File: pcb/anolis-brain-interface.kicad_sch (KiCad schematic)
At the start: 2 parts, among them U1 RHD2216, U2 Setebos-I

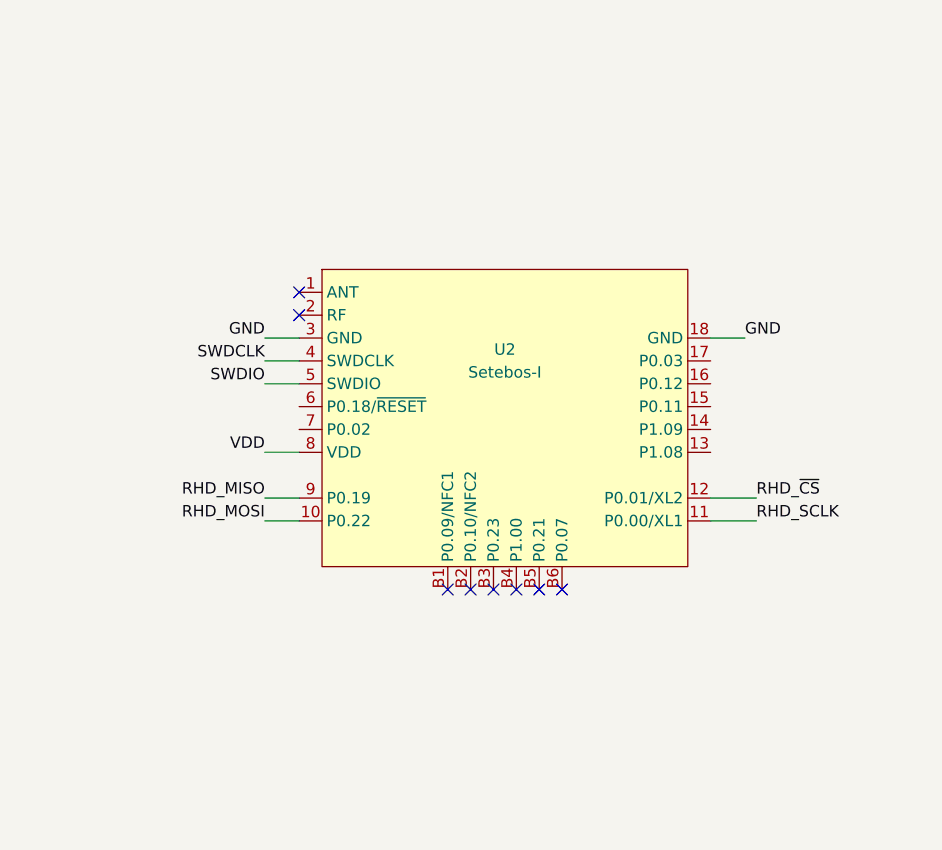
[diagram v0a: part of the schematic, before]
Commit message: Added uSD socket.
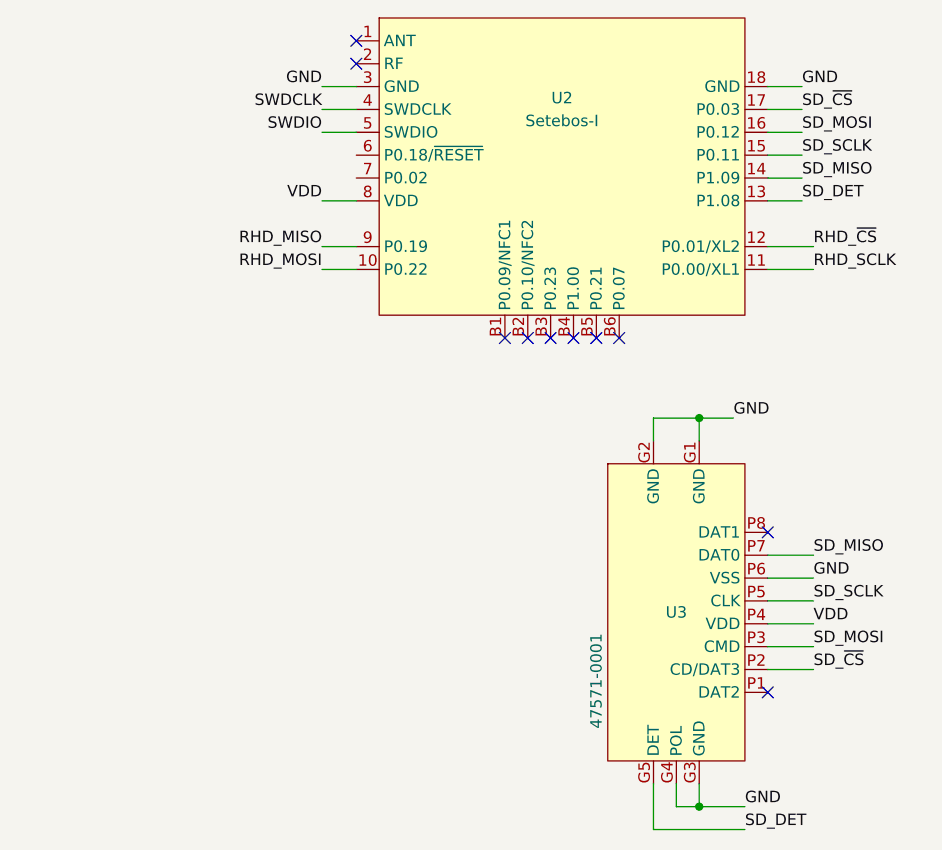
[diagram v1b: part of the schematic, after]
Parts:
- added U3: 47571-0001, sd:475710001, symbol sd:475710001
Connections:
- net GND: now also U3.G1 (GND), U3.G2 (GND), U3.G3 (GND), U3.G4 (POL), U3.P6 (VSS)
- net VDD: now also U3.P4 (VDD)
- net SD_DET: now reaches U2.13 (P1.08)
- net SD_DET: now also U3.G5 (DET)
- net SD_MISO: now reaches U2.14 (P1.09)
- net SD_MISO: now also U3.P7 (DAT0)
- net SD_SCLK: now reaches U2.15 (P0.11)
- net SD_SCLK: now also U3.P5 (CLK)
- net SD_MOSI: now reaches U2.16 (P0.12)
- net SD_MOSI: now also U3.P3 (CMD)
- net SD_~{CS}: now reaches U2.17 (P0.03)
- net SD_~{CS}: now also U3.P2 (CD/DAT3)
- no-connect marks 12 -> 14
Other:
- moved on the sheet: U2

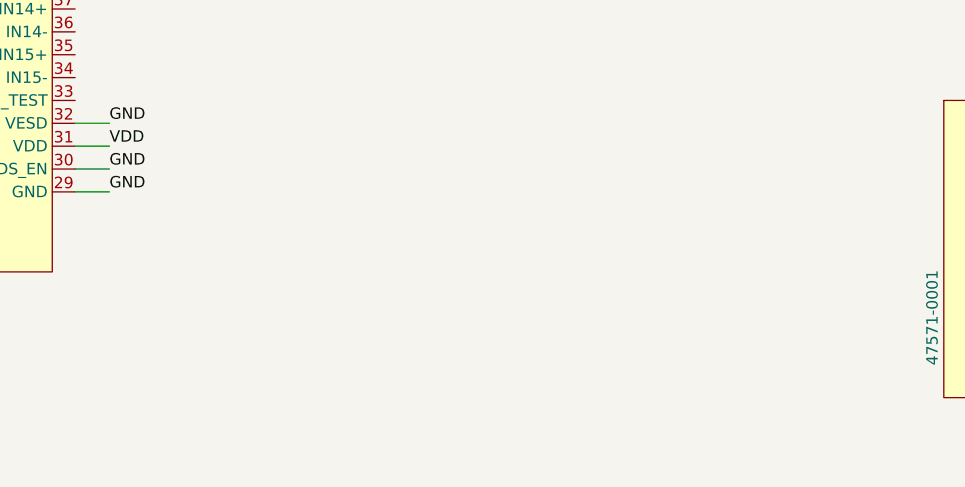
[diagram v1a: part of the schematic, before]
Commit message: Added power supply.
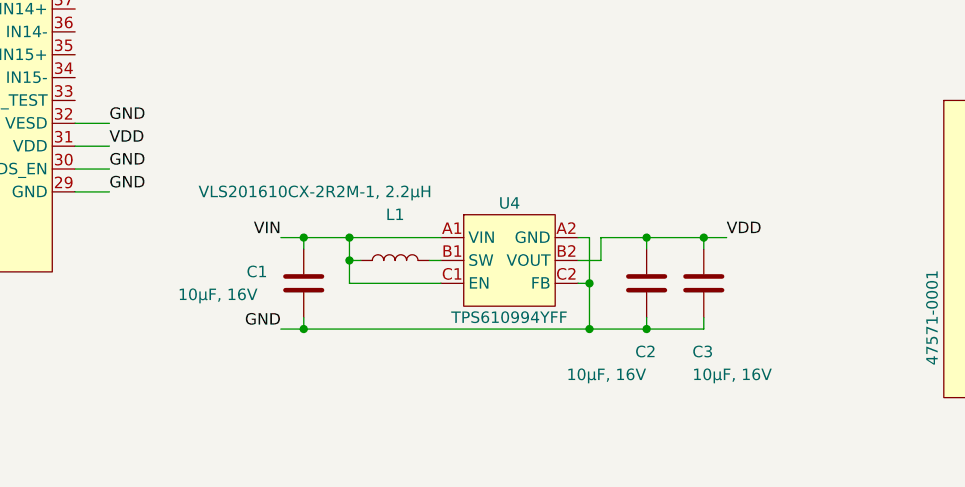
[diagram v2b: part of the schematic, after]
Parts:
- added C1, C2, C3: 10µF, 16V, Capacitor_SMD:C_0603_1608Metric, symbol Device:C
- added L1: VLS201610CX-2R2M-1, 2.2µH, Inductor_SMD:L_Murata_DFE201610P, symbol Device:L
- added U4: TPS610994YFF, Package_BGA:Texas_DSBGA-6_0.855x1.255mm_Layout2x3_P0.4mm_LevelC, symbol tps61099:TPS61099
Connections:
- net GND: now also C1.2, C2.2, C3.2, U4.A2 (GND), U4.C2 (FB)
- net VDD: now also C2.1, C3.1, U4.B2 (VOUT)
- new net: L1.2, U4.B1 (SW)
- new net VIN: C1.1, L1.1, U4.A1 (VIN), U4.C1 (EN)

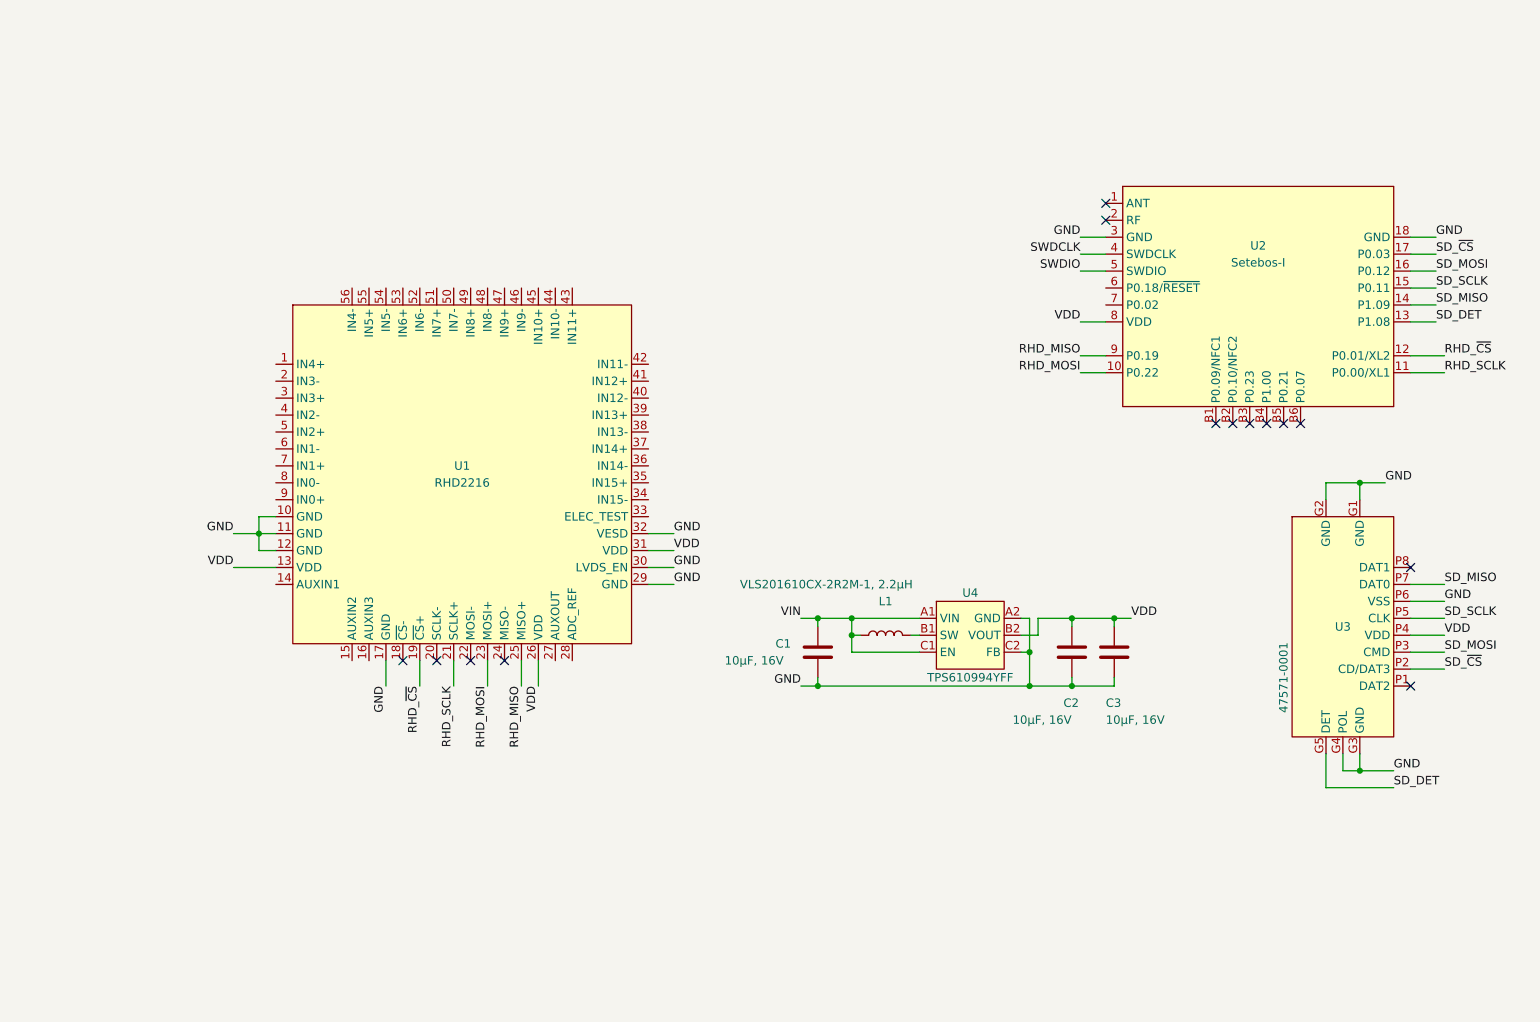
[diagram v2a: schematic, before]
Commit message: Added capacitors.
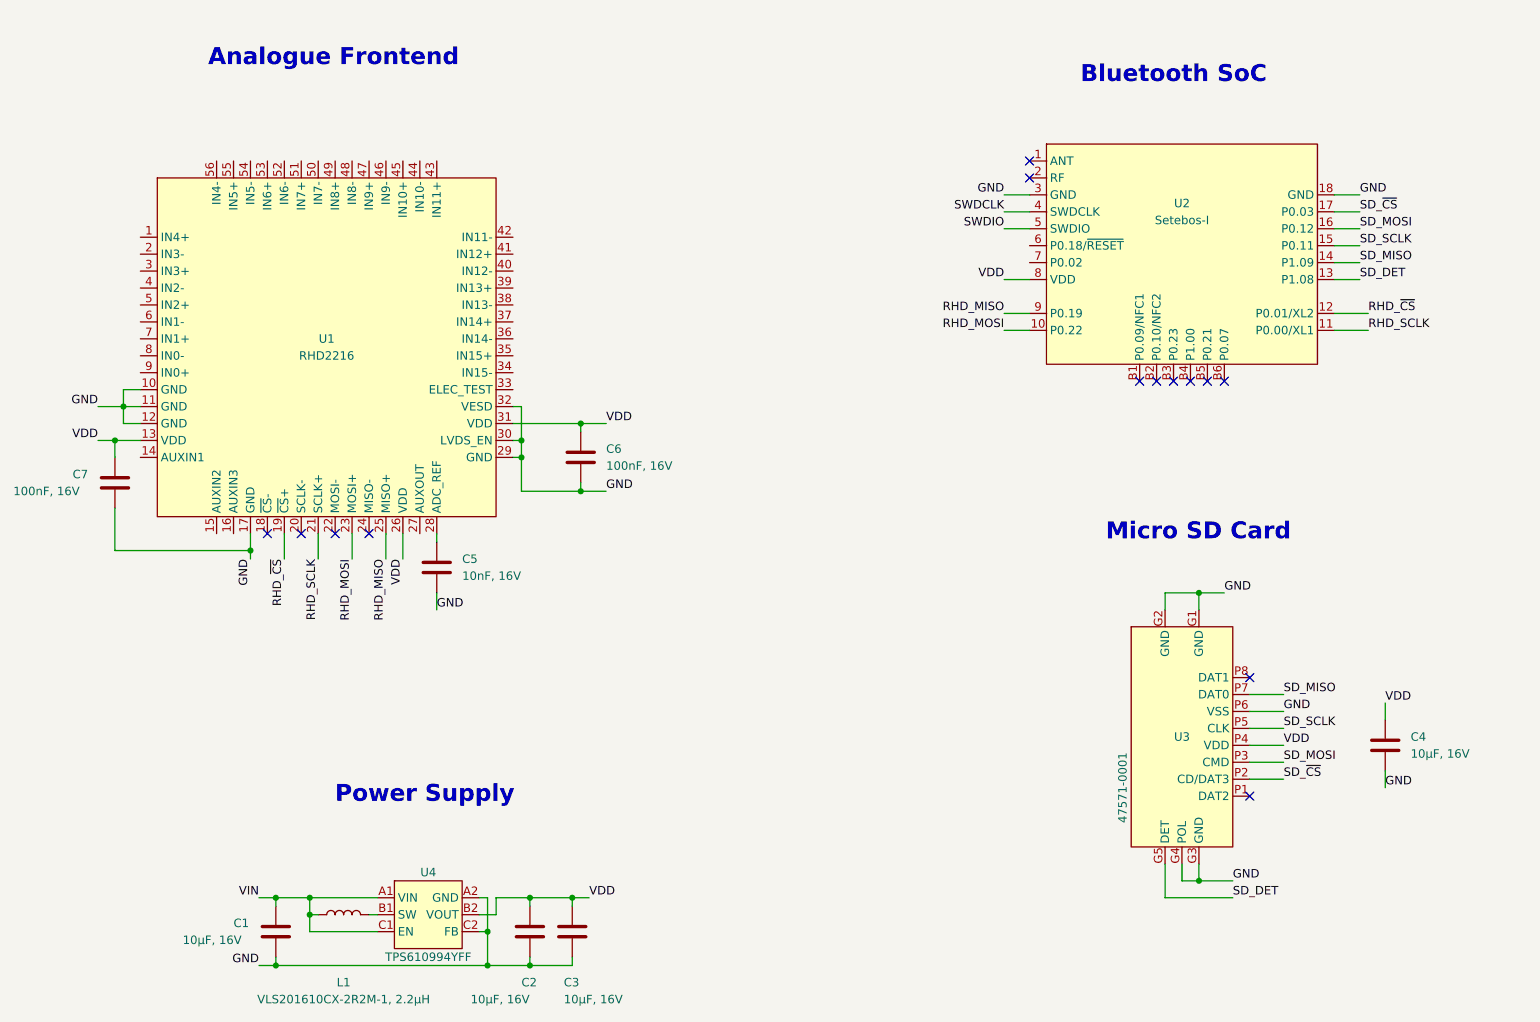
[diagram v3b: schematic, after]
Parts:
- added C4: 10µF, 16V, Capacitor_SMD:C_0603_1608Metric, symbol Device:C
- added C5: 10nF, 16V, Capacitor_SMD:C_0402_1005Metric, symbol Device:C
- added C6, C7: 100nF, 16V, Capacitor_SMD:C_0402_1005Metric, symbol Device:C
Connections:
- net GND: now also C4.2, C5.2, C6.2, C7.2
- net VDD: now also C4.1, C6.1, C7.1
- net at U1.28 (ADC_REF): now also C5.1
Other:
- note added: "Analogue Frontend"
- note added: "Bluetooth SoC"
- note added: "Micro SD Card"
- note added: "Power Supply"
- moved on the sheet: C1, C2, C3, L1, U1, U2, U3, U4

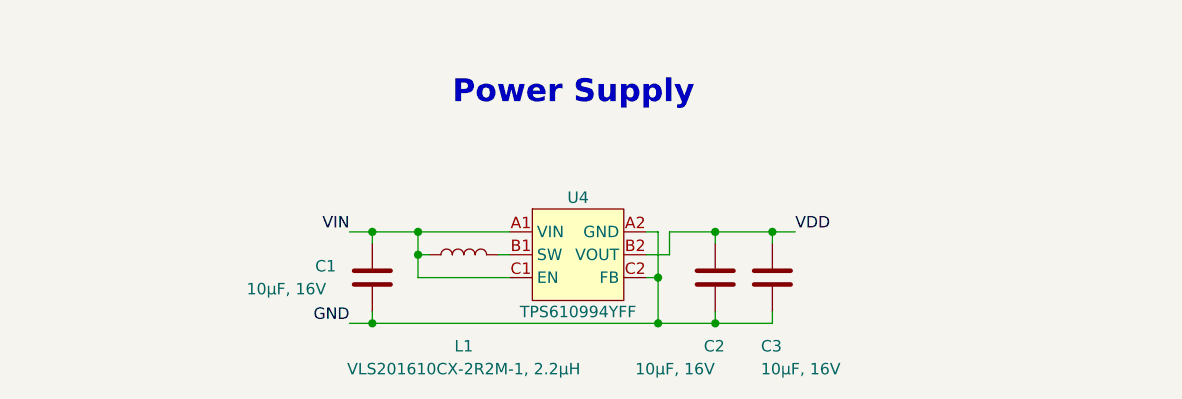
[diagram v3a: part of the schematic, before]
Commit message: Added battery connector.
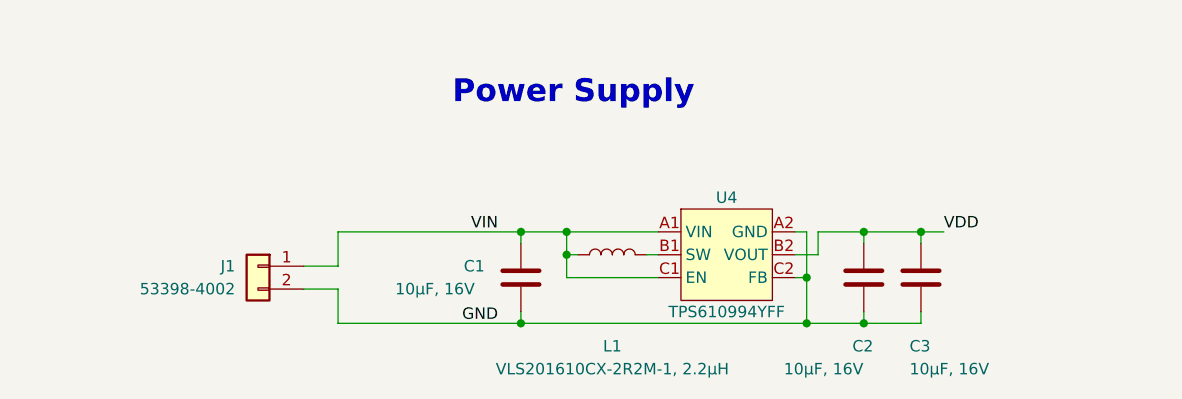
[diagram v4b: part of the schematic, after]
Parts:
- added J1: 53398-4002, Connector_Molex:Molex_PicoBlade_53398-0271_1x02-1MP_P1.25mm_Vertical, symbol Connector_Generic:Conn_01x02
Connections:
- net GND: now also J1.2 (Pin_2)
- net VIN: now also J1.1 (Pin_1)
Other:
- title: (none) -> Anolis Brain Interface
- moved on the sheet: C1, C2, C3, L1, U4

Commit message: Diode added.
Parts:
- added D1: PMEG2010EJ, Diode_SMD:D_SOD-323F, symbol Diode:PMEG2010EJ
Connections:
- net VIN: now also D1.1 (K); no longer J1.1 (Pin_1)
- new net: D1.2 (A), J1.1 (Pin_1)
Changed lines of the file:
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@@
+    (stroke (width 0) (type default))
+  )
+  (wire (pts (xy 59.69 154.94) (xy 68.58 154.94))
     (stroke (width 0) (type default))
   )
@@
     (stroke (width 0) (type default))
   )
-  (wire (pts (xy 48.26 154.94) (xy 68.58 154.94))
+  (wire (pts (xy 48.26 154.94) (xy 52.07 154.94))
     (stroke (width 0) (type default))
   )
@@
         )
       )
+    )
+  )
+  (symbol (lib_id "Diode:PMEG2010EJ") (at 55.88 154.94 180) (unit 1)
+    (in_bom yes) (on_board yes) (dnp no) (fields_autoplaced)
+    (property "Reference" "D1" (at 56.1975 148.59 0)
+      (effects (font (size 1.27 1.27)))
+    )
+    (property "Value" "PMEG2010EJ" (at 56.1975 151.13 0)
+      (effects (font (size 1.27 1.27)))
+    )
+    (property "Footprint" "Diode_SMD:D_SOD-323F" (at 55.88 150.495 0)
+      (effects (font (size 1.27 1.27)) hide)
+    )
+    (property "Datasheet" "https://assets.nexperia.com/documents/data-sheet/PMEG2010EH_EJ_ET.pdf" (at 55.88 154.94 0)
+      (effects (font (size 1.27 1.27)) hide)
+    )
+    (pin "1")
+    (pin "2")
+    (instances
+      (project "anolis-brain-interface"
+        (path "/2073a088-93fe-4857-bf83-cba62e9d9994"
+          (reference "D1") (unit 1)
+        )
+      )

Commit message: Segmented draft.
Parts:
- removed C4: 10µF, 16V, Capacitor_SMD:C_0603_1608Metric, symbol Device:C
- removed U3: 47571-0001, sd:475710001, symbol sd:475710001
- added BT1: Battery_Cell, Battery:BatteryHolder_Keystone_3000_1x12mm, symbol Device:Battery_Cell
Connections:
- net SD_MISO is gone; now on net RHD_MISO: U2.14 (P1.09)
- net SD_MOSI is gone; now on net RHD_SCLK: U2.16 (P0.12)
- net SD_SCLK is gone; now on net RHD_MOSI: U2.15 (P0.11)
- net SD_~{CS} is gone; now on net RHD_~{CS}: U2.17 (P0.03)
- net RHD_MISO: no longer U2.9 (P0.19)
- net RHD_MOSI: no longer U2.10 (P0.22)
- net RHD_SCLK: no longer U2.11 (P0.00/XL1)
- net RHD_~{CS}: no longer U2.12 (P0.01/XL2)
- net SD_DET: no longer names the net of U2.13 (P1.08)
- no-connect marks 14 -> 13
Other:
- note removed: "Micro SD Card"

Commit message: New PCB design.
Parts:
- removed BT1: Battery_Cell, Battery:BatteryHolder_Keystone_3000_1x12mm, symbol Device:Battery_Cell
- removed D1: PMEG2010EJ, Diode_SMD:D_SOD-323F, symbol Diode:PMEG2010EJ
- removed L1: VLS201610CX-2R2M-1, 2.2µH, Inductor_SMD:L_Murata_DFE201610P, symbol Device:L
- removed U4: TPS610994YFF, Package_BGA:Texas_DSBGA-6_0.855x1.255mm_Layout2x3_P0.4mm_LevelC, symbol tps61099:TPS61099
- added TP1, TP2, TP3, TP4, TP5, TP6, TP7, TP8, TP9: TestPoint, TestPoint:TestPoint_Pad_1.0x1.0mm, symbol Connector:TestPoint
- added U3: TPS70933, Package_TO_SOT_SMD:SOT-23-5, symbol tps709:TPS70933
- J1: footprint Connector_Molex:Molex_PicoBlade_53398-0271_1x02-1MP_P1.25mm_Vertical -> zero-hachi:214721-0020
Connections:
- net GND: now also U3.2 (GND)
- net VDD: now also U3.5 (OUT)
- net VIN: now also J1.1 (Pin_1), U3.1 (IN), U3.3 (EN)
- net at U1.1 (IN4+): now also TP1.1
- net at U1.2 (IN3-): now also U1.3 (IN3+), U1.34 (IN15-), U1.35 (IN15+), U1.36 (IN14-), U1.37 (IN14+), U1.38 (IN13-), U1.39 (IN13+), U1.4 (IN2-), U1.40 (IN12-), U1.41 (IN12+), U1.42 (IN11-), U1.44 (IN10-), U1.46 (IN9-), U1.48 (IN8-), U1.5 (IN2+), U1.50 (IN7-), U1.52 (IN6-), U1.54 (IN5-), U1.56 (IN4-), U1.6 (IN1-), U1.7 (IN1+), U1.8 (IN0-), U1.9 (IN0+), TP9.1
- net at U1.43 (IN11+): now also TP8.1
- net at U1.45 (IN10+): now also TP7.1
- net at U1.47 (IN9+): now also TP6.1
- net at U1.49 (IN8+): now also TP5.1
- net at U1.51 (IN7+): now also TP4.1
- net at U1.53 (IN6+): now also TP3.1
- net at U1.55 (IN5+): now also TP2.1
- no-connect marks 13 -> 14

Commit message: PCB done.
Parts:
- added BAT+1, BAT-1: TestPoint, TestPoint:TestPoint_Pad_1.0x1.0mm, symbol Connector:TestPoint
- added D1: BAT54CW, Package_TO_SOT_SMD:SOT-323_SC-70, symbol Diode:BAT54CW
- added D2: LED, LED_SMD:LED_0402_1005Metric, symbol Device:LED
- added R1: 50k, Resistor_SMD:R_0402_1005Metric, symbol Device:R
- added R2: 1k, Resistor_SMD:R_0402_1005Metric, symbol Device:R
- added SW1: EVQ-P7A01P, Button_Switch_SMD:SW_SPST_EVQP7A, symbol Switch:SW_SPST
- added U4: LTC4054ES5-4.2, Package_TO_SOT_SMD:TSOT-23-5, symbol Battery_Management:LTC4054ES5-4.2
- IN1: renamed from TP1; now left out of the parts list
- IN2: renamed from TP2; now left out of the parts list
- IN3: renamed from TP3; now left out of the parts list
- IN4: renamed from TP4; now left out of the parts list
- IN5: renamed from TP5; now left out of the parts list
- IN6: renamed from TP6; now left out of the parts list
- IN7: renamed from TP7; now left out of the parts list
- IN8: renamed from TP8; now left out of the parts list
- J1: value 53398-4002 -> 214721-0020; Order Number (none) -> 538-214721-0020; Supplier (none) -> Mouser
- REF1: renamed from TP9; now left out of the parts list
- U1: Order Number (none) -> RHD2216; Supplier (none) -> Intan
- U2: footprint setebos:setebos -> setebos:setebos-no-drc; Order Number (none) -> 3868806; Supplier (none) -> Farnell
- U3: footprint Package_TO_SOT_SMD:SOT-23-5 -> Package_TO_SOT_SMD:TSOT-23-5; Order Number (none) -> 595-TPS70933DBVR; Supplier (none) -> Mouser
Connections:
- net GND: now also BAT-1.1, R1.2, R2.2, U4.2 (GND)
- net RHD_MISO: now also U2.11 (P0.00/XL1); no longer U2.14 (P1.09)
- net RHD_MOSI: now also U2.10 (P0.22); no longer U2.15 (P0.11)
- net RHD_SCLK: now also U2.9 (P0.19); no longer U2.16 (P0.12)
- net RHD_~{CS}: now also U2.12 (P0.01/XL2); no longer U2.17 (P0.03)
- net VDD: no longer C2.1
- net VIN: now also C2.1, D1.3; no longer C1.1, J1.1 (Pin_1)
- net at U2.13 (P1.08): now also D2.2 (A)
- net ~{CHRG}: now reaches U2.7 (P0.02)
- net ~{CHRG}: now also U4.1 (~{CHRG})
- new net: BAT+1.1, SW1.2 (B), U4.3 (BAT)
- new net: D2.1 (K), R2.1
- new net: R1.1, U4.5 (PROG)
- new net: D1.2, SW1.1 (A)
- new net 5V: C1.1, D1.1, J1.1 (Pin_1), U4.4 (V_{CC})
- no-connect marks 14 -> 18
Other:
- moved on the sheet: C1, C2, C5, C6, C7, IN1, IN2, IN3, IN4, IN5, IN6, IN7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
